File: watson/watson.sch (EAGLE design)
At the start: 37 parts, among them X1 2540-FLAT

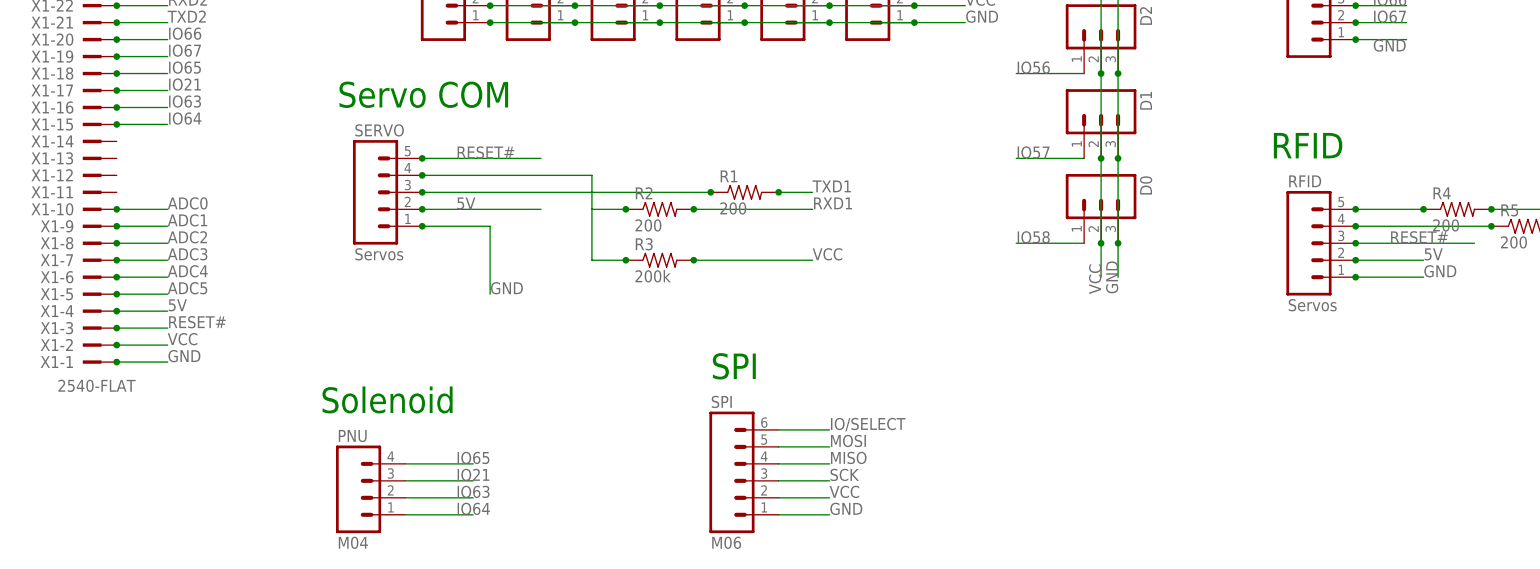
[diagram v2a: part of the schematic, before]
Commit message: Updated and fixed Sherlock and Watson to Rev C
- Changed RFID to SIMPLE, SPI to RFID on Watson.
- Added extra pin to RFID for interrupts (on Sherlock and Watson).

- Added 7-pin MTA connector to Eagle library.

- Added 0805 LED to Eagle library.

- Replaced LEDs on Sherlock to 0805 LEDs.

- Fixed version numbers and silkscreen on both boards.

DFM for SherlocK: https://www.freedfm.com/freedfm/0019486703397689/results/summary2.htm
DFM for Watson: https://www.freedfm.com/freedfm/0019486703397690/results/summary2.htm

Change-Id: Ib97956c76452f7ac388d76660bbab957bcb45fe9
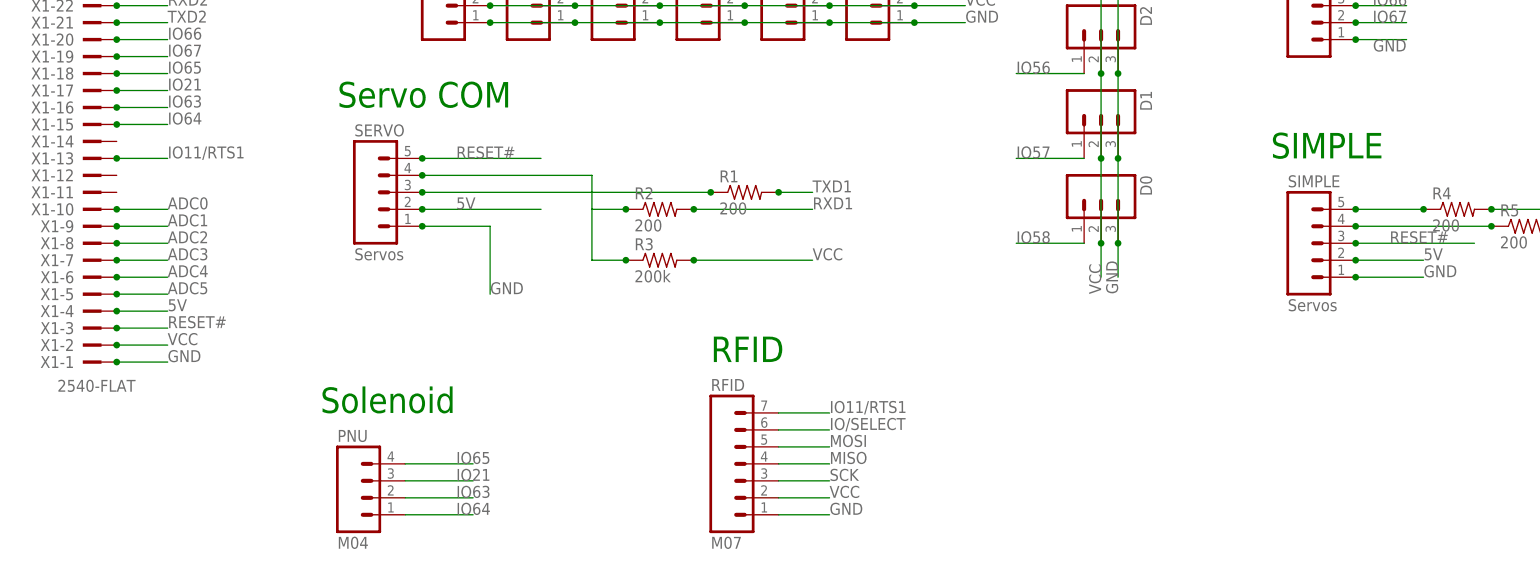
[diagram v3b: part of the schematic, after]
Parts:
- removed SPI: M06, MTA-connectors:M06
- added SIMPLE: Servos, MTA-connectors:M05
- RFID: value Servos -> M07; device MTA-connectors:M05 -> pie:M07
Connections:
- new net IO11/RTS1: RFID.7, X1-13.KL
- net 5V: now also SIMPLE.2; no longer RFID.2
- net GND: now also SIMPLE.1; no longer SPI.1
- net IO/SELECT: now also RFID.6; no longer SPI.6
- net MISO: now also RFID.4; no longer SPI.4
- net MOSI: now also RFID.5; no longer SPI.5
- net N$5: now also SIMPLE.5; no longer RFID.5
- net N$6: now also SIMPLE.4; no longer RFID.4
- net RESET#: now also SIMPLE.3; no longer RFID.3
- net SCK: now also RFID.3; no longer SPI.3
- net VCC: now also RFID.2; no longer SPI.2
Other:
- note added: "SIMPLE"
- note removed: "SPI"
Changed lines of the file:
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@@
 <?xml version="1.0" encoding="utf-8"?>
 <!DOCTYPE eagle SYSTEM "eagle.dtd">
-<eagle version="6.2">
+<eagle version="6.3">
 <drawing>
 <settings>
@@
 <part name="I2C1" library="MTA-connectors" deviceset="M04" device=""/>
 <part name="I2C0" library="MTA-connectors" deviceset="M04" device=""/>
-<part name="SPI" library="MTA-connectors" deviceset="M06" device=""/>
+<part name="RFID" library="pie" deviceset="M07" device=""/>
 <part name="R1" library="resistor" deviceset="R-US_" device="R0603" value="200"/>
 <part name="R2" library="resistor" deviceset="R-US_" device="R0603" value="200"/>
@@
 <attribute name="OC_FARNELL" value="unknown"/>
 </part>
-<part name="RFID" library="MTA-connectors" deviceset="M05" device="" value="Servos"/>
+<part name="SIMPLE" library="MTA-connectors" deviceset="M05" device="" value="Servos"/>
 <part name="PNU" library="MTA-connectors" deviceset="M04" device=""/>
 <part name="R5" library="resistor" deviceset="R-US_" device="R0603" value="200"/>
@@
 <part name="FRAME1" library="pie" deviceset="FRAME-LETTER" device="">
 <attribute name="AUTHOR" value="Michael C., Sumita G., Sahar M."/>
-<attribute name="REVISION" value="A"/>
+<attribute name="REVISION" value="C"/>
 </part>
 </parts>
@@
 <text x="53.34" y="78.74" size="3.81" layer="91">Servo COM</text>
 <text x="66.04" y="175.26" size="3.81" layer="91">I2C Sensor</text>
-<text x="109.22" y="38.1" size="3.81" layer="91">SPI</text>
-<text x="193.04" y="71.12" size="3.81" layer="91">RFID</text>
+<text x="109.22" y="40.64" size="3.81" layer="91">RFID</text>
+<text x="193.04" y="71.12" size="3.81" layer="91">SIMPLE</text>
 <text x="50.8" y="33.02" size="3.81" layer="91">Solenoid</text>
 </plain>
@@
 <instance part="I2C1" gate="G$1" x="71.12" y="165.1"/>
 <instance part="I2C0" gate="G$1" x="58.42" y="165.1"/>
-<instance part="SPI" gate="G$1" x="114.3" y="25.4"/>
+<instance part="RFID" gate="G$1" x="114.3" y="25.4"/>
 <instance part="R1" gate="G$1" x="114.3" y="66.04"/>
 <instance part="R2" gate="G$1" x="101.6" y="63.5"/>
@@
 <instance part="X1" gate="-39" x="15.24" y="137.16" rot="MR180"/>
 <instance part="X1" gate="-40" x="15.24" y="139.7" rot="MR180"/>
-<instance part="RFID" gate="G$1" x="200.66" y="60.96"/>
+<instance part="SIMPLE" gate="G$1" x="200.66" y="60.96"/>
 <instance part="PNU" gate="G$1" x="58.42" y="22.86"/>
 <instance part="R5" gate="G$1" x="231.14" y="60.96"/>
@@
 </segment>
 <segment>
-<pinref part="SPI" gate="G$1" pin="1"/>
+<pinref part="RFID" gate="G$1" pin="1"/>
 <wire x1="119.38" y1="17.78" x2="127" y2="17.78" width="0.1524" layer="91"/>
 <label x="127" y="17.78" size="1.778" layer="95"/>
@@
 </segment>
 <segment>
-<pinref part="RFID" gate="G$1" pin="1"/>
+<pinref part="SIMPLE" gate="G$1" pin="1"/>
 <wire x1="205.74" y1="53.34" x2="215.9" y2="53.34" width="0.1524" layer="91"/>
 <junction x="205.74" y="53.34"/>
@@
 </segment>
 <segment>
-<pinref part="SPI" gate="G$1" pin="2"/>
+<pinref part="RFID" gate="G$1" pin="2"/>
 <wire x1="119.38" y1="20.32" x2="127" y2="20.32" width="0.1524" layer="91"/>
 <label x="127" y="20.32" size="1.778" layer="95"/>
@@
 <net name="MOSI" class="0">
 <segment>
-<pinref part="SPI" gate="G$1" pin="5"/>
+<pinref part="RFID" gate="G$1" pin="5"/>
 <wire x1="119.38" y1="27.94" x2="127" y2="27.94" width="0.1524" layer="91"/>
 <label x="127" y="27.94" size="1.778" layer="95"/>
@@
 <net name="MISO" class="0">
 <segment>
-<pinref part="SPI" gate="G$1" pin="4"/>
+<pinref part="RFID" gate="G$1" pin="4"/>
 <wire x1="119.38" y1="25.4" x2="127" y2="25.4" width="0.1524" layer="91"/>
 <label x="127" y="25.4" size="1.778" layer="95"/>
@@
 <net name="SCK" class="0">
 <segment>
-<pinref part="SPI" gate="G$1" pin="3"/>
+<pinref part="RFID" gate="G$1" pin="3"/>
 <wire x1="119.38" y1="22.86" x2="127" y2="22.86" width="0.1524" layer="91"/>
 <label x="127" y="22.86" size="1.778" layer="95"/>
@@
 </segment>
 <segment>
-<pinref part="RFID" gate="G$1" pin="3"/>
+<pinref part="SIMPLE" gate="G$1" pin="3"/>
 <wire x1="205.74" y1="58.42" x2="223.52" y2="58.42" width="0.1524" layer="91"/>
 <junction x="205.74" y="58.42"/>
@@
 </segment>
 <segment>
-<pinref part="RFID" gate="G$1" pin="2"/>
+<pinref part="SIMPLE" gate="G$1" pin="2"/>
 <wire x1="205.74" y1="55.88" x2="215.9" y2="55.88" width="0.1524" layer="91"/>
 <junction x="205.74" y="55.88"/>
@@
 <net name="IO/SELECT" class="0">
 <segment>
-<pinref part="SPI" gate="G$1" pin="6"/>
+<pinref part="RFID" gate="G$1" pin="6"/>
 <wire x1="119.38" y1="30.48" x2="127" y2="30.48" width="0.1524" layer="91"/>
 <label x="127" y="30.48" size="1.778" layer="95"/>
@@
 <net name="N$5" class="0">
 <segment>
-<pinref part="RFID" gate="G$1" pin="5"/>
+<pinref part="SIMPLE" gate="G$1" pin="5"/>
 <wire x1="205.74" y1="63.5" x2="215.9" y2="63.5" width="0.1524" layer="91"/>
 <pinref part="R4" gate="G$1" pin="1"/>
@@
 <net name="N$6" class="0">
 <segment>
-<pinref part="RFID" gate="G$1" pin="4"/>
+<pinref part="SIMPLE" gate="G$1" pin="4"/>
 <pinref part="R5" gate="G$1" pin="1"/>
 <wire x1="205.74" y1="60.96" x2="226.06" y2="60.96" width="0.1524" layer="91"/>
@@
 </segment>
 </net>
+<net name="IO11/RTS1" class="0">
+<segment>
+<pinref part="X1" gate="-13" pin="KL"/>
+<wire x1="20.32" y1="71.12" x2="27.94" y2="71.12" width="0.1524" layer="91"/>
+<junction x="20.32" y="71.12"/>
+<label x="27.94" y="71.12" size="1.778" layer="95"/>
+</segment>
+<segment>
+<pinref part="RFID" gate="G$1" pin="7"/>
+<wire x1="119.38" y1="33.02" x2="127" y2="33.02" width="0.1524" layer="91"/>
+<label x="127" y="33.02" size="1.778" layer="95"/>
+</segment>
+</net>

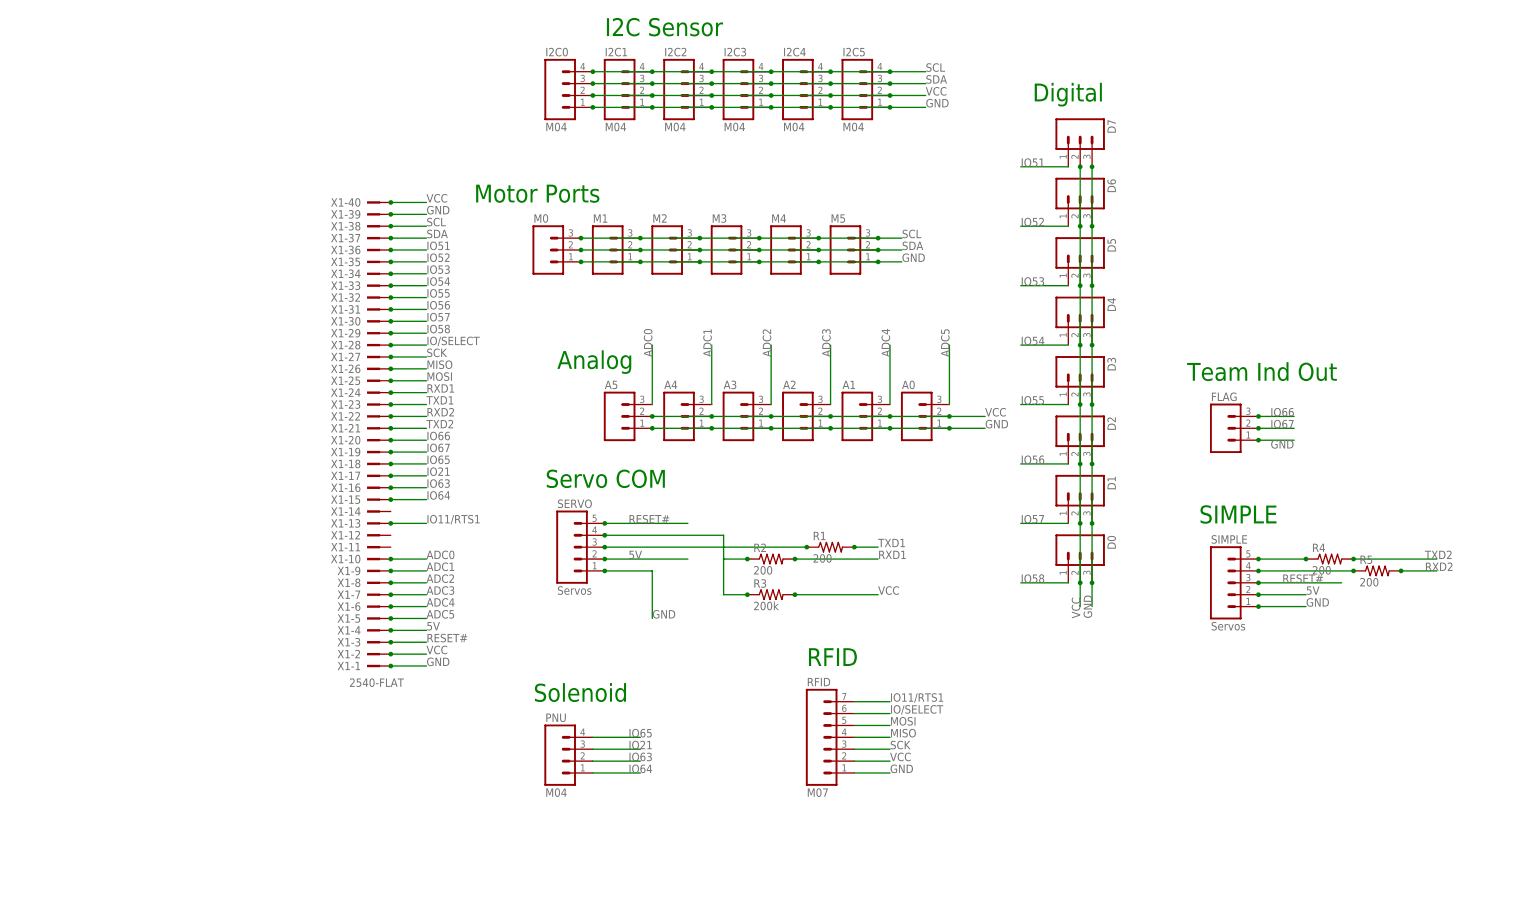
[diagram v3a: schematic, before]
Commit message: Updated Sherlock, Watson & Solenoid Board to Rev D. Updated pie.lbr.
- Put SSOP16 footprint and symbol (from Sparkfun.lbr) in pie.lbr.
  Can be used as a template for any SSOP16 device.
- Created SSOP14 footprint and symbol in pie.lbr using SSOP16.
  Can be used as a template for any SSOP14 device.
- Added QUADNOR device to pie.lbr
- Added VCC and enable pin to solenoid connector on Watson
- Added enable pin for solenoid board on Sherlock
- Added quad-NOR gate onto Solenoid Board
- Added VCC and enable pin for quad-NOR gate on Solenoid Board
- Added 0.1uF capacitors between VCC&GND and 12V&GND for Solenoid Board
- Added mounting holes to Solenoid Board
- Added additional holes to Sherlock and Watson for the testing jig
- Replaced all holes with standoff part in pie.lbr
- Gave each hole a value, either "Mounting", "Test" or "Mounting + Test"
  to state their purpose.
- Added/copied devices on boards that were NOT in pie.lbr TO pie.lbr
- Removed unnecessary packages from copied devices
- Manually set pad diameters for through-hole packages that were
  added/created/already there for these three boards
- Added PARTNUMBER attribute to the library parts added/copied/
  created/already there for these three boards
- Moved all Sherlock passives to the top

RYAN: I fixed what you asked for this revision. If this goes
through, I will then work on fixing everything else you told me to.

Sherlock DFM: https://www.freedfm.com/freedfm/0019486703414971/results/summary2.htm
Watson DFM: https://www.freedfm.com/freedfm/0019486703414975/results/summary2.htm
Solenoid Board DFM: https://www.freedfm.com/freedfm/0019486703414973/results/summary2.htm

Change-Id: Ie6b1bdecadde8b7bc780ad23041f2e110bf24a4c
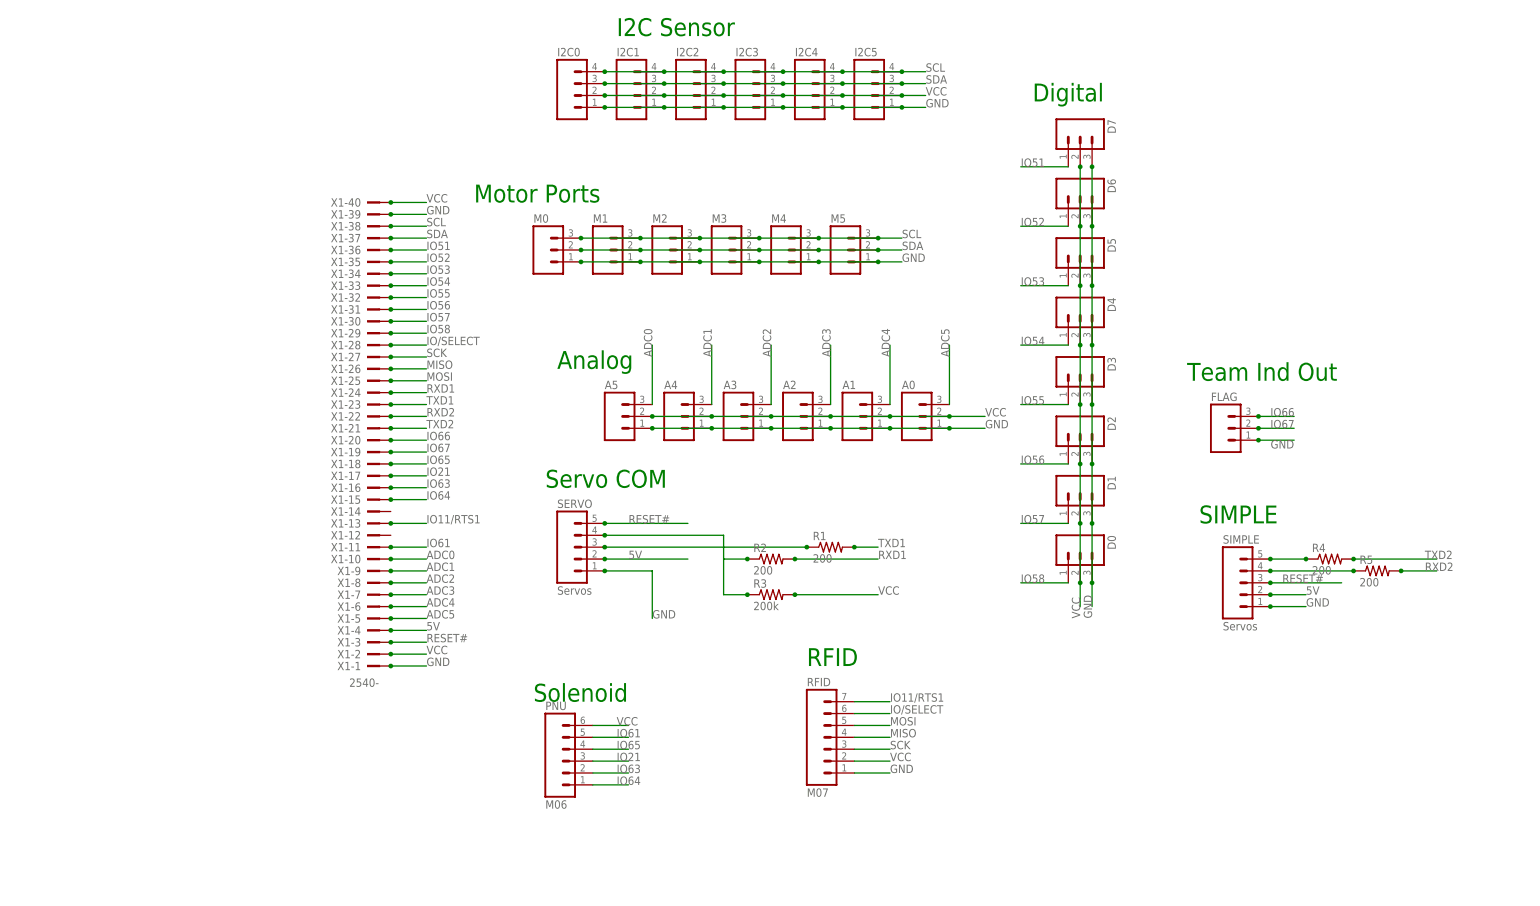
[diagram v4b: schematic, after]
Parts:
- A0, A1, A2, A3, A4, A5, D0, D1, D2, D3, D4, D5, D6, D7, FLAG, M0, M1, M2, M3, M4, M5: device pie:M03MTA1X3 -> pie:M031X03-MTA
- I2C0, I2C1, I2C2, I2C3, I2C4, I2C5: value M04 -> (none); device MTA-connectors:M04 -> pie:M041X04-MTA
- PNU: value M04 -> M06; device MTA-connectors:M04 -> pie:M06
- R1, R2, R3, R4, R5: device resistor:R-US_R0603 -> pie:R-US_R0603
- SERVO, SIMPLE: device MTA-connectors:M05 -> pie:M05MTA
- X1: value 2540-FLAT -> 2540-; device pie:2540-FLAT -> pie:2540-
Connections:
- new net IO61: PNU.5, X1-11.KL
- net VCC: now also PNU.6
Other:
- moved on the sheet: I2C0, I2C1, I2C2, I2C3, I2C4, I2C5, SIMPLE
